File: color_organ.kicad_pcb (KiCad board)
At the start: 2 copper layers, 110.2 x 116.8 mm, 125 parts, among them CON1 BARREL_JACK, J1 Audio_3.5mm, Q1 2N3904, Q2 2N3904, Q3 2N3904, Q4 2N3904, Q5 2N3904, Q6 2N3904, SW1 SPST, U1 MC33204P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

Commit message: Initial board design done.
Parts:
- moved R27 134.9 mm to (55.9, 146.1), turned to 0 degrees
- moved R24 129.7 mm to (55.9, 142.2), turned to 0 degrees
- moved R28 123.0 mm to (81.3, 146.1), turned to 0 degrees
- moved R25 117.9 mm to (81.3, 142.2), turned to 0 degrees
- moved C16 109.4 mm to (69.8, 144.2), turned to 270 degrees
- moved C17 106.5 mm to (66.7, 144.1), turned to 270 degrees
- moved D10 106.2 mm to (61.2, 35.8)
- moved D11 106.2 mm to (61.2, 27.7)
- moved D4 106.2 mm to (52.6, 35.8)
- moved D5 106.2 mm to (52.6, 27.7)
- moved R29 104.3 mm to (105.4, 146.1), turned to 0 degrees
- moved R26 99.5 mm to (105.4, 142.2), turned to 0 degrees
- moved RV4 97.5 mm to (57.1, 133.3), turned to 180 degrees
- moved R18 96.7 mm to (52.7, 45.1), turned to 270 degrees
- moved R4 96.2 mm to (55.9, 62.2), turned to 0 degrees
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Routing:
- net Net-(C6-Pad1): track 0.00 -> 136.6 mm, vias 0 -> 1
- net Net-(C11-Pad1): track 0.00 -> 120.7 mm
- net Net-(C20-Pad1): track 0.00 -> 110.2 mm
- net Net-(C2-Pad1): track 0.00 -> 102.0 mm, vias 0 -> 2
- net Net-(C28-Pad1): track 0.00 -> 101.6 mm, vias 0 -> 1
- net Net-(C1-Pad1): track 0.00 -> 96.0 mm, vias 0 -> 6
- net Net-(C12-Pad1): track 0.00 -> 91.0 mm, vias 0 -> 1
- net Net-(C5-Pad1): track 0.00 -> 87.2 mm, vias 0 -> 1
- net Net-(C21-Pad1): track 0.00 -> 71.7 mm, vias 0 -> 1
- net Net-(R13-Pad2): track 32.8 -> 100.1 mm, vias 0 -> 1
- net Net-(C3-Pad1): track 0.00 -> 62.7 mm, vias 0 -> 1
- net Net-(C27-Pad1): track 0.00 -> 51.9 mm
- net Net-(C13-Pad1): track 0.00 -> 51.7 mm
- net Net-(C14-Pad1): track 29.9 -> 80.0 mm, vias 0 -> 1
- net Net-(C4-Pad1): track 0.00 -> 49.7 mm, vias 0 -> 1
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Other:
- board size 110.2 x 116.8 mm -> 96.5 x 170.2 mm

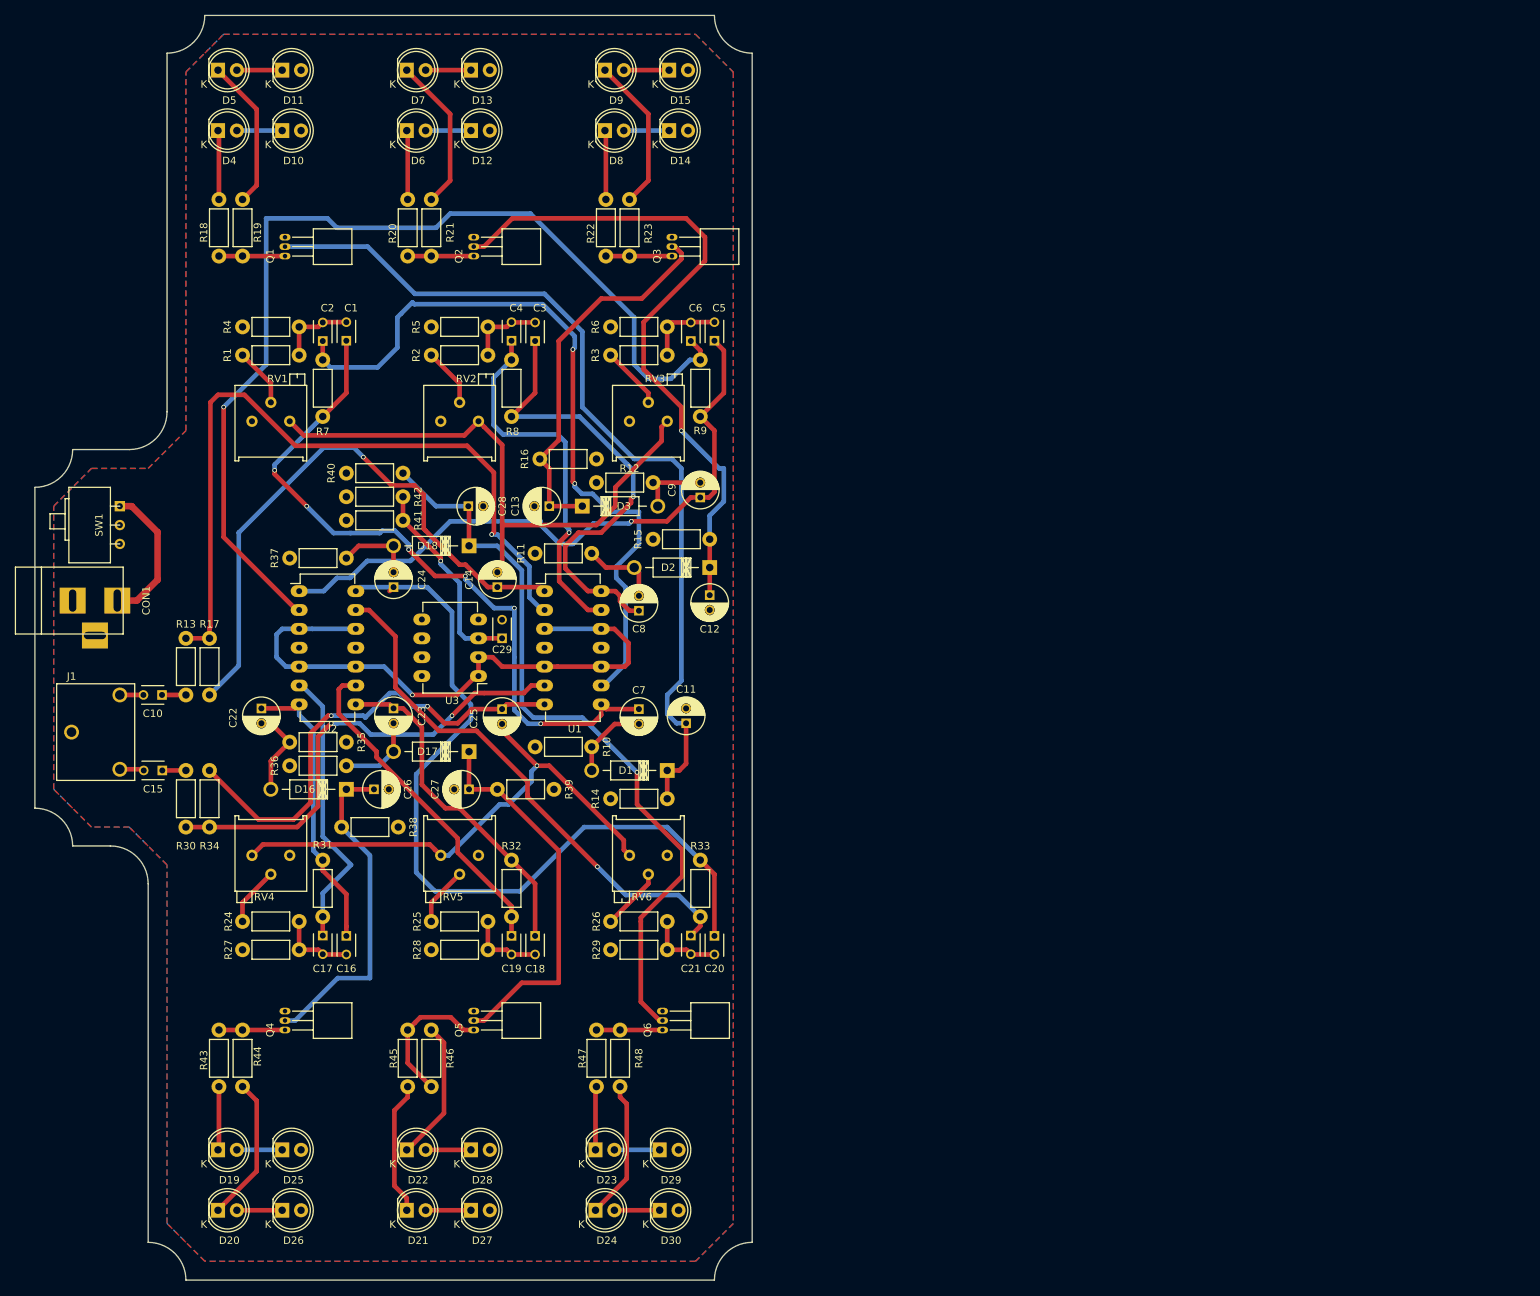
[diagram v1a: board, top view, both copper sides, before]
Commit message: Updated board to meet OSH Park design rules
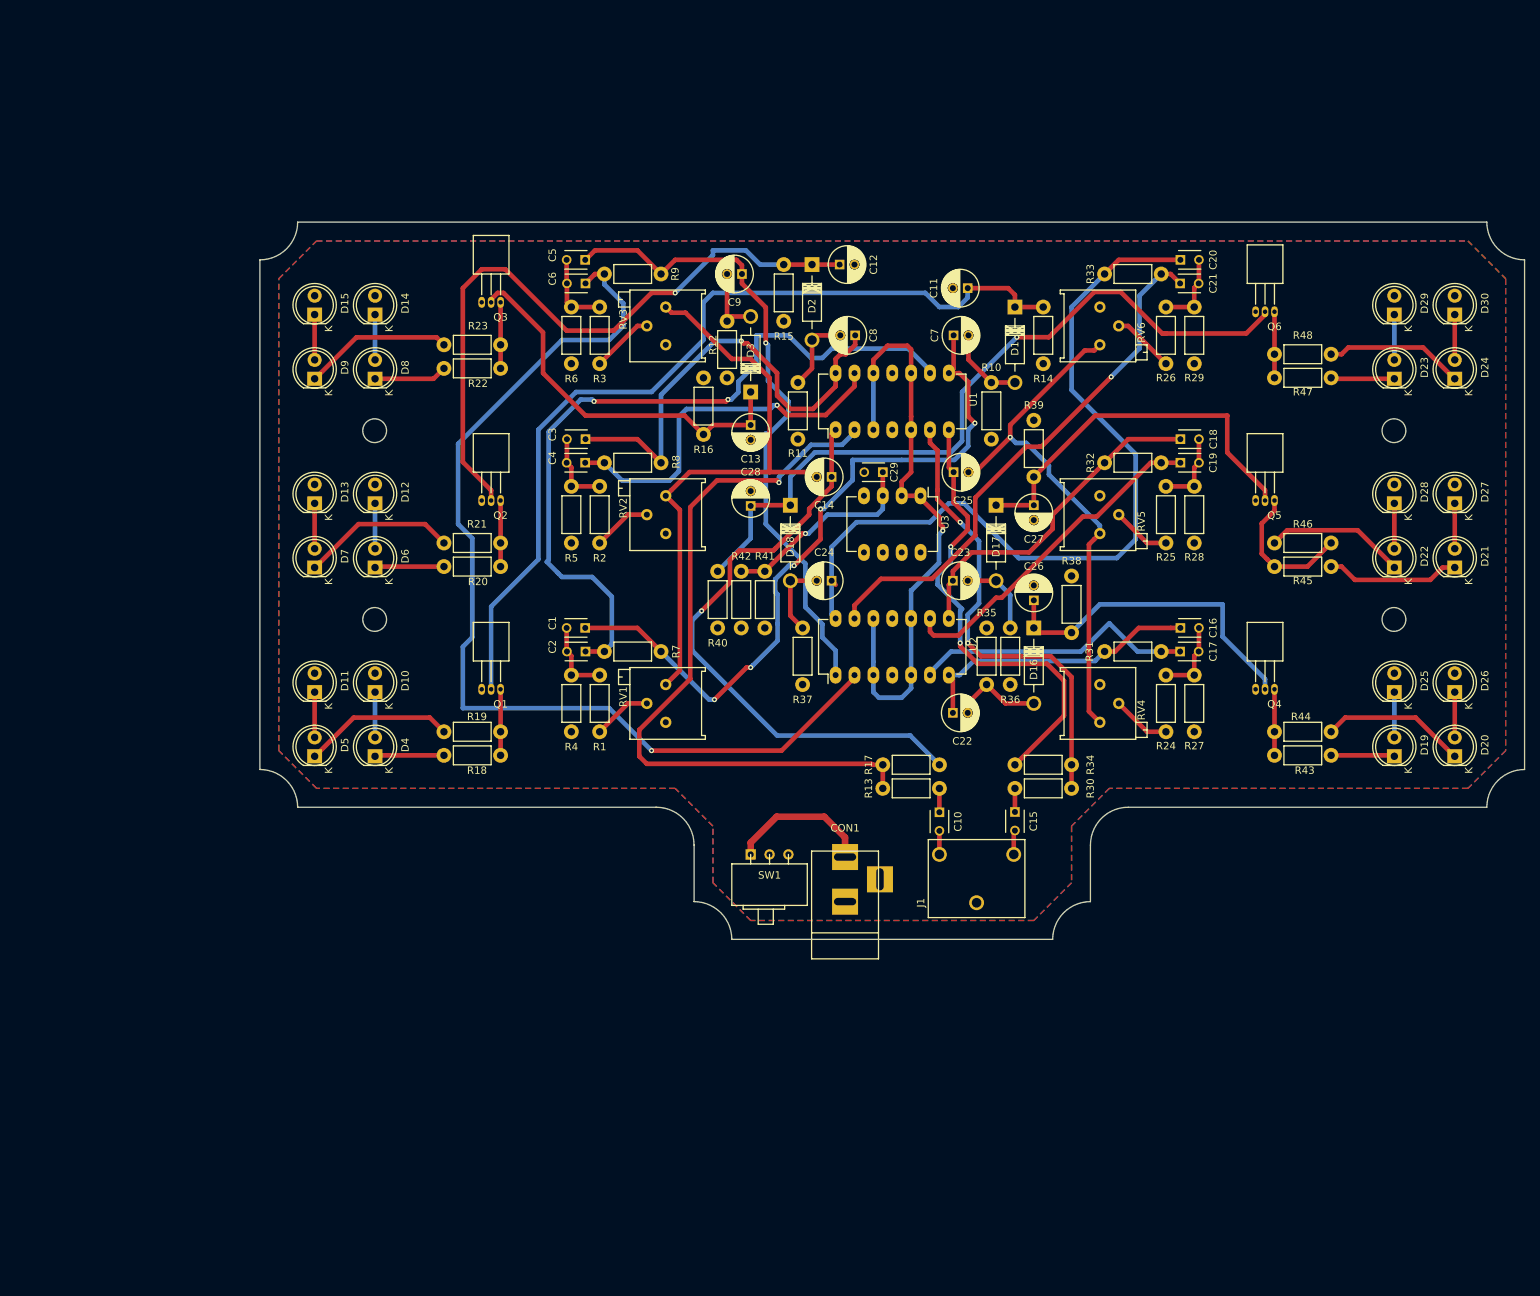
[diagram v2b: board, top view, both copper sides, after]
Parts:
- added REF**: MountingHole_3.2mm_M3, Mounting_Holes:MountingHole_3.2mm_M3, F.Cu at (210.8, 76.2)
- added REF**: MountingHole_3.2mm_M3, Mounting_Holes:MountingHole_3.2mm_M3, F.Cu at (210.8, 101.6)
- added REF**: MountingHole_3.2mm_M3, Mounting_Holes:MountingHole_3.2mm_M3, F.Cu at (73.7, 101.6)
- added REF**: MountingHole_3.2mm_M3, Mounting_Holes:MountingHole_3.2mm_M3, F.Cu at (73.7, 76.2)
- moved D20 177.3 mm to (219.0, 120.0), turned to 90 degrees
- moved D26 172.5 mm to (219.0, 111.4), turned to 90 degrees
- moved D19 166.9 mm to (210.9, 120.0), turned to 90 degrees
- moved D21 165.4 mm to (219.0, 94.6), turned to 90 degrees
- moved D27 163.0 mm to (219.0, 86.0), turned to 90 degrees
- moved D25 161.8 mm to (210.9, 111.4), turned to 90 degrees
- moved D30 161.2 mm to (219.0, 60.6), turned to 90 degrees
- moved D24 160.9 mm to (219.0, 69.2), turned to 90 degrees
- moved R43 156.2 mm to (202.4, 119.9), turned to 180 degrees
- moved D22 154.3 mm to (210.9, 94.6), turned to 90 degrees
- moved R44 154.1 mm to (202.4, 116.7), turned to 180 degrees
- moved D28 151.7 mm to (210.9, 86.0), turned to 90 degrees
- moved D29 149.7 mm to (210.9, 60.6), turned to 90 degrees
- moved D23 149.4 mm to (210.9, 69.2), turned to 90 degrees
- moved R45 142.6 mm to (202.4, 94.5), turned to 180 degrees
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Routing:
- net Net-(D9-Pad1): track 20.9 -> 20.1 mm
- net Net-(C1-Pad1): track 96.0 -> 96.8 mm, vias 6 -> 5
- net Net-(D8-Pad1): track 9.32 -> 10.0 mm
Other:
- board size 96.5 x 170.2 mm -> 170.2 x 96.5 mm
- net class Default: via_dia 0.6 -> 0.6858; via_drill 0.4 -> 0.3302
- net class PWR: via_dia 0.6 -> 0.6858; via_drill 0.4 -> 0.3302
- rule trace_min: 0.2 -> 0.1524
- rule via_min_drill: 0.3 -> 0.3302
- rule via_min_size: 0.4 -> 0.6858

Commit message: Updated mounting holes
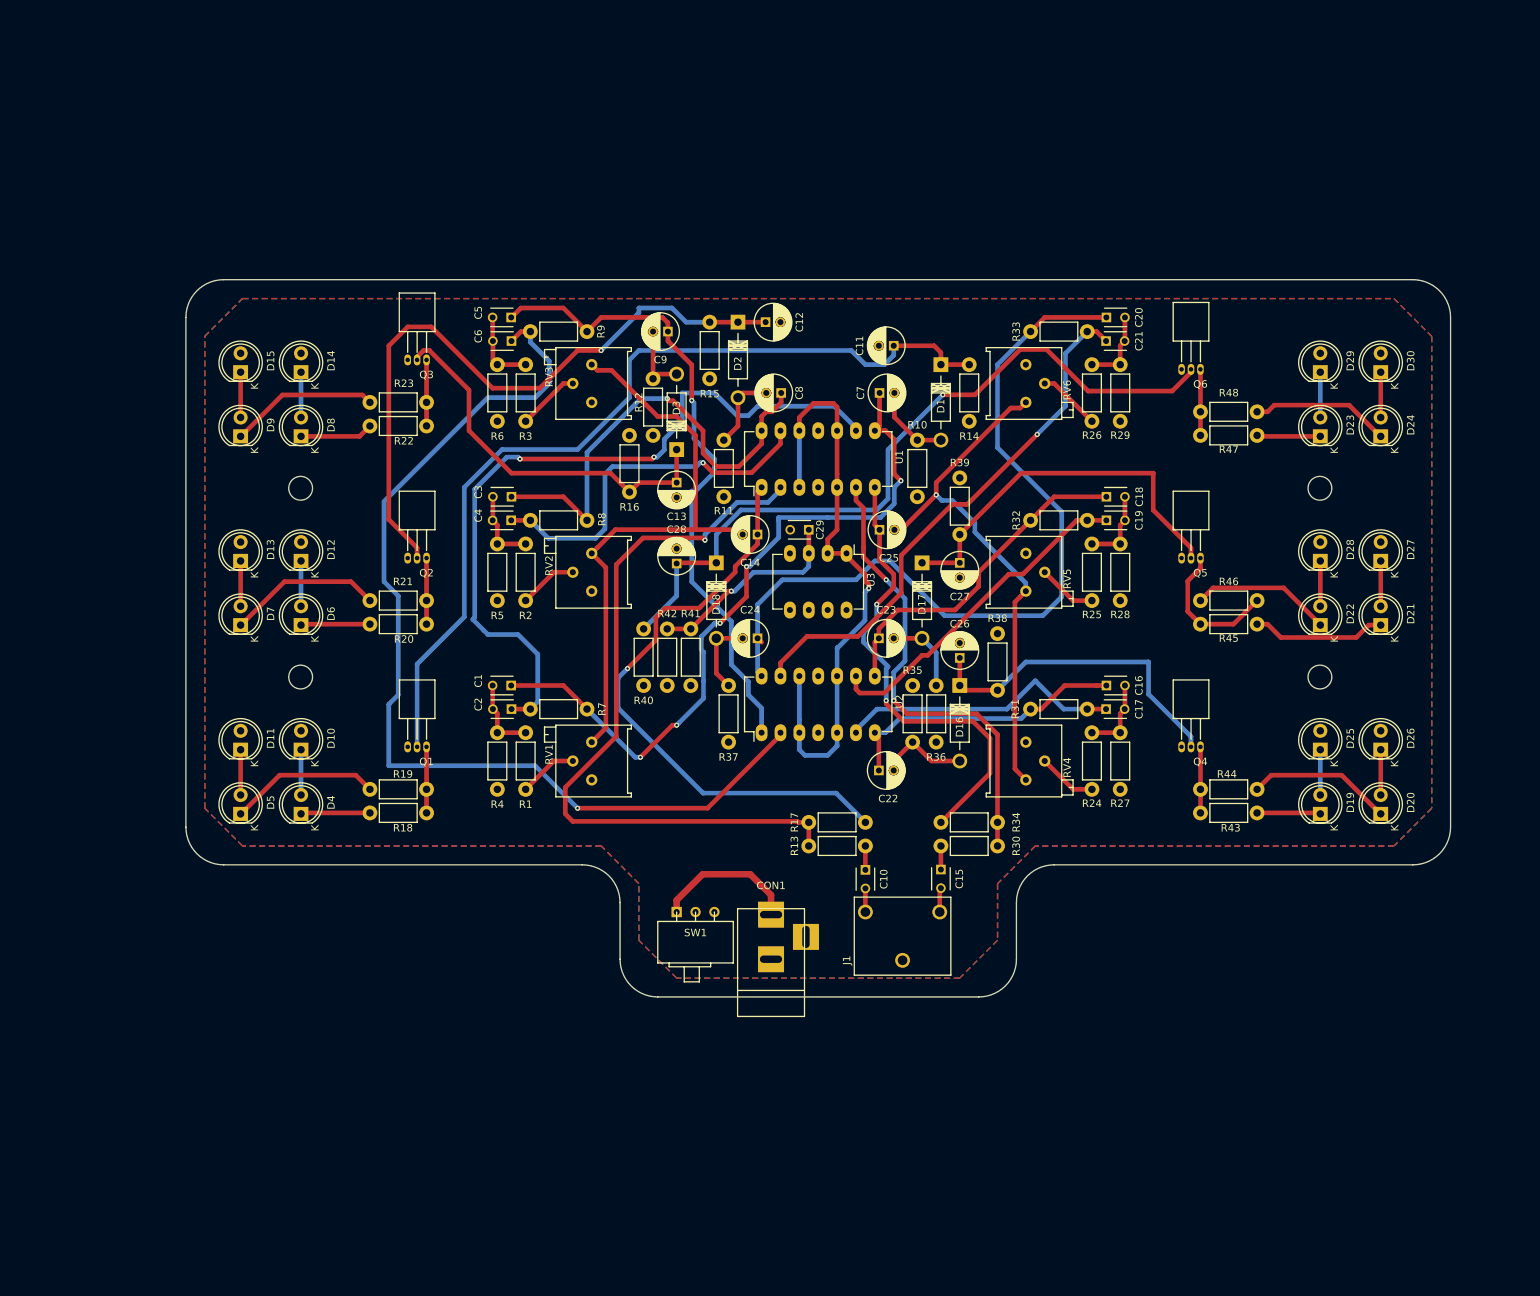
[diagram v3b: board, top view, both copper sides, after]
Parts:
- moved C15 12.6 mm to (149.9, 135.3)
- moved R17 12.6 mm to (132.1, 128.9)
- moved R34 12.6 mm to (157.5, 128.9)
- moved D14 12.6 mm to (63.8, 68.3)
- moved D29 12.6 mm to (200.9, 68.3)
- moved Q6 12.6 mm to (184.8, 67.9)
- moved C10 12.6 mm to (139.7, 135.3)
- moved C14 12.6 mm to (125.2, 90.2)
- moved C16 12.6 mm to (172.1, 110.5)
- moved C18 12.6 mm to (172.1, 85.1)
- moved C19 12.6 mm to (172.1, 88.3)
- moved C2 12.6 mm to (92.1, 113.7)
- moved C20 12.6 mm to (172.1, 61.0)
- moved C22 12.6 mm to (141.5, 121.9)
- moved C23 12.6 mm to (141.5, 104.1)
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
